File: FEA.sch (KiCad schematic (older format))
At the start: 18 parts

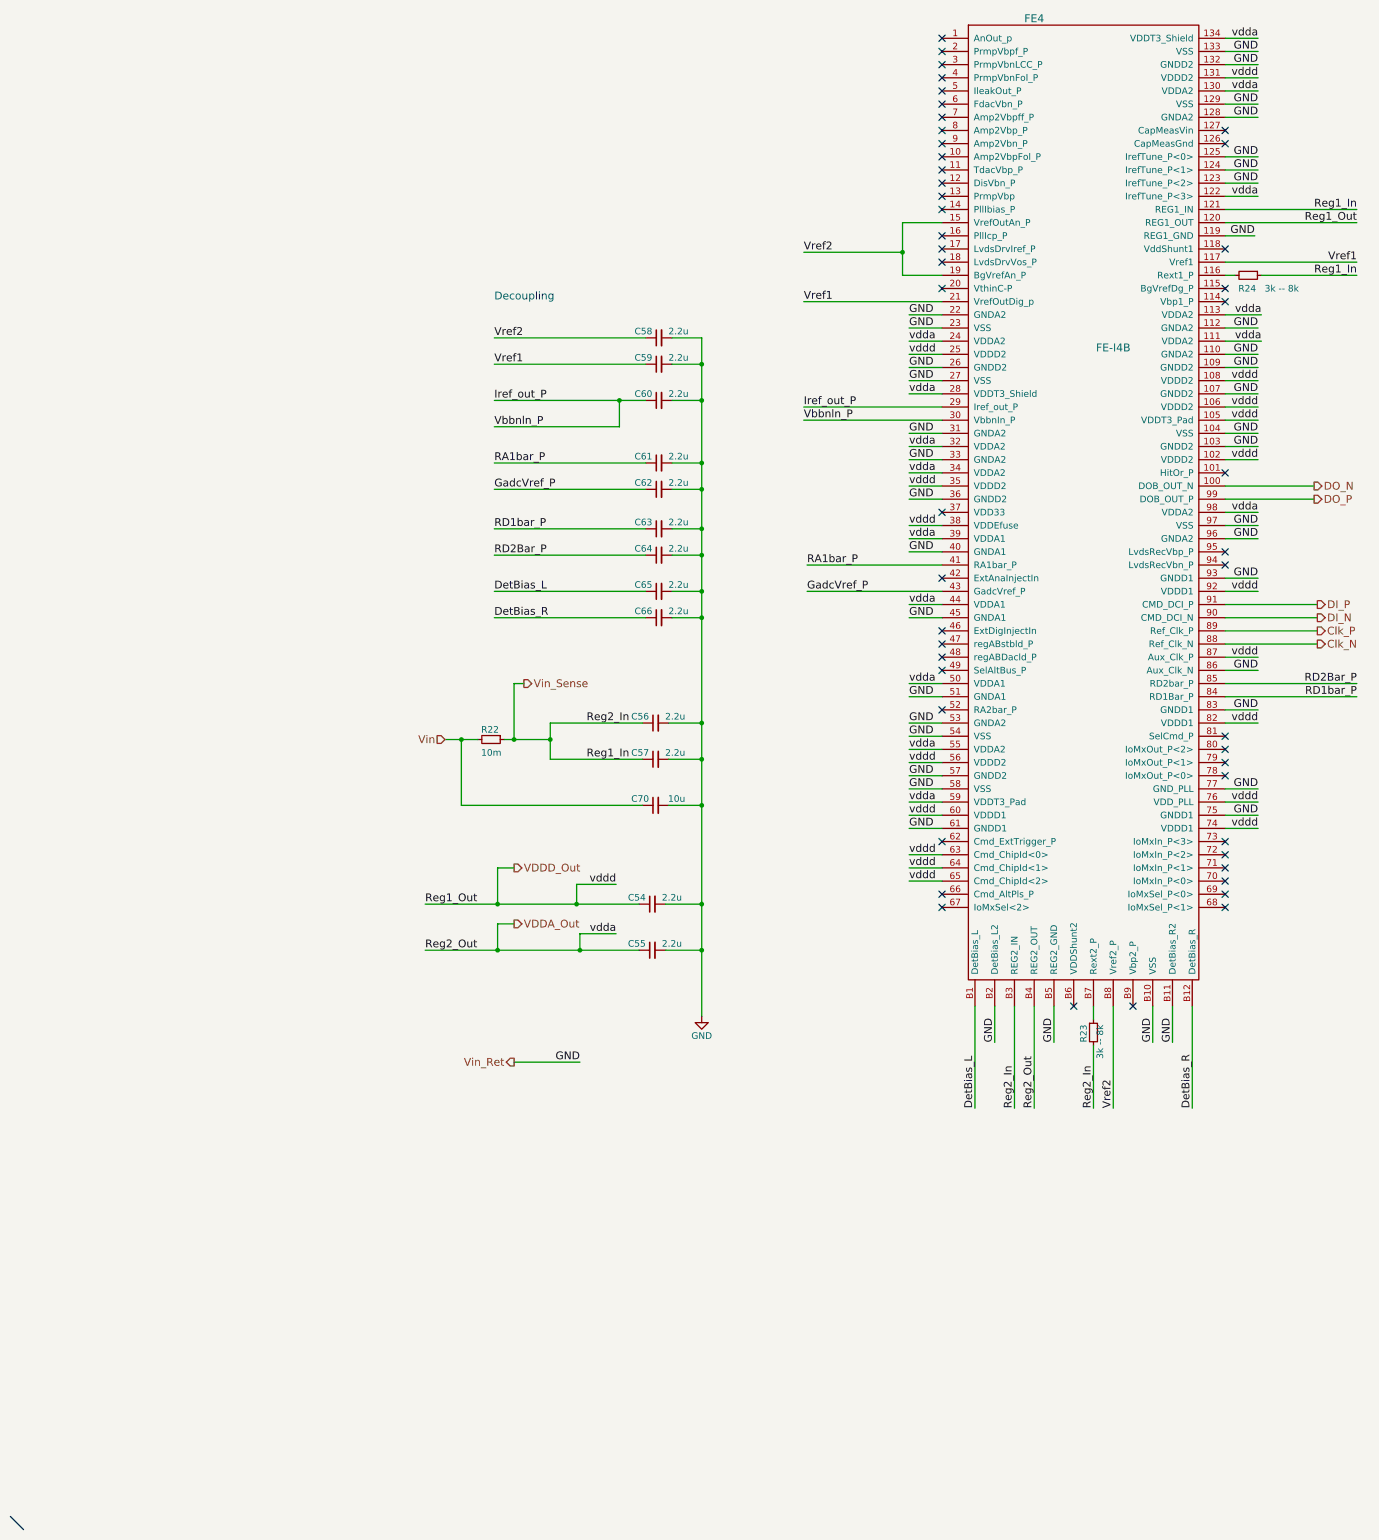
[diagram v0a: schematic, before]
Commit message: Edit decoupling cap values for V/I ref and Regulators
Signed-off-by: Katie Dunne <kdunne@mail.ccsf.edu>
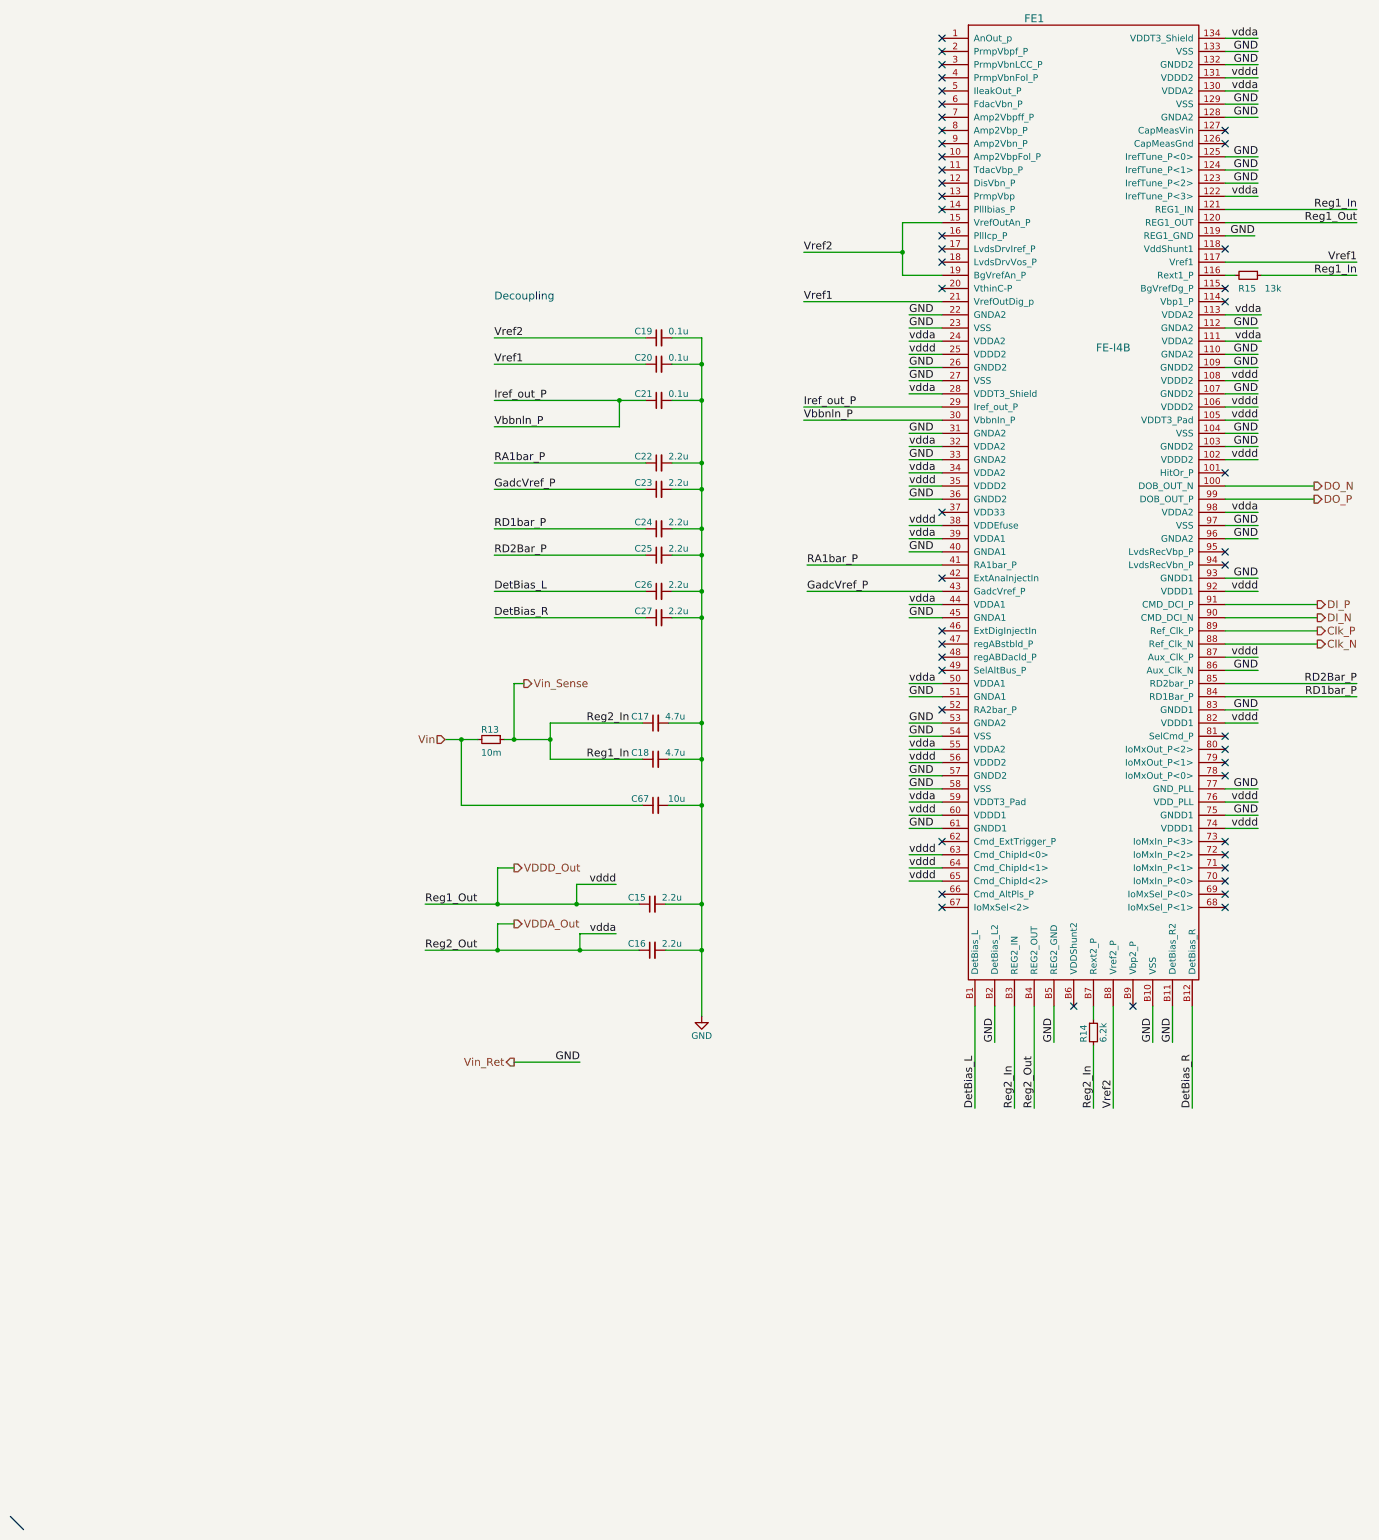
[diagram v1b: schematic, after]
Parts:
- C17, C18: value 2.2u -> 4.7u
- C19, C20, C21: value 2.2u -> 0.1u
- R14: value 3k -- 8k -> 6.2k
- R15: value 3k -- 8k -> 13k
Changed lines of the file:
@@
 $Descr A4 8268 11693 portrait
 encoding utf-8
-Sheet 5 5
+Sheet 2 5
 Title ""
 Date ""
@@
 AR Path="/58B026BA/589D45EA" Ref="FE3"  Part="1"
 AR Path="/58B026C4/589D45EA" Ref="FE4"  Part="1"
-F 0 "FE4" H 5225 4275 60  0000 C CNN
+F 0 "FE1" H 5225 4275 60  0000 C CNN
 F 1 "FE-I4B" H 5825 1775 60  0000 C CNN
 F 2 "module:WirebondPads" H 5825 2525 60  0001 C CNN
@@
 AR Path="/58B026BA/58AFC93B" Ref="R20"  Part="1"
 AR Path="/58B026C4/58AFC93B" Ref="R23"  Part="1"
-F 0 "R23" V 5600 8400 50  0000 L CNN
-F 1 "3k -- 8k" V 5725 8275 50  0000 L CNN
+F 0 "R14" V 5600 8400 50  0000 L CNN
+F 1 "6.2k" V 5750 8400 50  0000 L CNN
 F 2 "Resistors_SMD:R_0402" H 5675 8475 50  0001 C CNN
 F 3 "" H 5675 8475 50  0001 C CNN
@@
 AR Path="/58B026BA/58AFD85E" Ref="R21"  Part="1"
 AR Path="/58B026C4/58AFD85E" Ref="R24"  Part="1"
-F 0 "R24" V 6950 2650 50  0000 L CNN
-F 1 "3k -- 8k" V 6950 2850 50  0000 L CNN
+F 0 "R15" V 6950 2650 50  0000 L CNN
+F 1 "13k" V 6950 2850 50  0000 L CNN
 F 2 "Resistors_SMD:R_0402" H 6850 2725 50  0001 C CNN
 F 3 "" H 6850 2725 50  0001 C CNN
@@
 AR Path="/58B026BA/58BA4BDB" Ref="#PWR06"  Part="1"
 AR Path="/58B026C4/58BA4BDB" Ref="#PWR07"  Part="1"
-F 0 "#PWR07" H 2700 8100 50  0001 C CNN
+F 0 "#PWR04" H 2700 8100 50  0001 C CNN
 F 1 "GND" H 2700 8200 50  0000 C CNN
 F 2 "" H 2700 8350 50  0001 C CNN
@@
 AR Path="/58B026BA/58BA843C" Ref="C45"  Part="1"
 AR Path="/58B026C4/58BA843C" Ref="C58"  Part="1"
-F 0 "C58" V 2425 3250 50  0000 L CNN
-F 1 "2.2u" V 2425 2975 50  0000 L CNN
+F 0 "C19" V 2425 3250 50  0000 L CNN
+F 1 "0.1u" V 2425 2975 50  0000 L CNN
 F 2 "Capacitors_SMD:C_0402" H 2375 3200 50  0001 C CNN
 F 3 "" H 2375 3200 50  0001 C CNN
@@
 AR Path="/58B026BA/58B3509B" Ref="R19"  Part="1"
 AR Path="/58B026C4/58B3509B" Ref="R22"  Part="1"
-F 0 "R22" V 1025 6175 50  0000 L CNN
+F 0 "R13" V 1025 6175 50  0000 L CNN
 F 1 "10m" V 1200 6175 50  0000 L CNN
 F 2 "Resistors_SMD:R_0603" H 1100 6250 50  0001 C CNN
@@
 AR Path="/58B026BA/58B81EC6" Ref="C46"  Part="1"
 AR Path="/58B026C4/58B81EC6" Ref="C59"  Part="1"
-F 0 "C59" V 2425 3450 50  0000 L CNN
-F 1 "2.2u" V 2425 3175 50  0000 L CNN
+F 0 "C20" V 2425 3450 50  0000 L CNN
+F 1 "0.1u" V 2425 3175 50  0000 L CNN
 F 2 "Capacitors_SMD:C_0402" H 2375 3400 50  0001 C CNN
 F 3 "" H 2375 3400 50  0001 C CNN
@@
 AR Path="/58B026BA/58B81EFE" Ref="C47"  Part="1"
 AR Path="/58B026C4/58B81EFE" Ref="C60"  Part="1"
-F 0 "C60" V 2425 3725 50  0000 L CNN
-F 1 "2.2u" V 2425 3450 50  0000 L CNN
+F 0 "C21" V 2425 3725 50  0000 L CNN
+F 1 "0.1u" V 2425 3450 50  0000 L CNN
 F 2 "Capacitors_SMD:C_0402" H 2375 3675 50  0001 C CNN
 F 3 "" H 2375 3675 50  0001 C CNN
@@
 AR Path="/58B026BA/58B81F3D" Ref="C48"  Part="1"
 AR Path="/58B026C4/58B81F3D" Ref="C61"  Part="1"
-F 0 "C61" V 2425 4200 50  0000 L CNN
+F 0 "C22" V 2425 4200 50  0000 L CNN
 F 1 "2.2u" V 2425 3925 50  0000 L CNN
 F 2 "Capacitors_SMD:C_0402" H 2375 4150 50  0001 C CNN
@@
 AR Path="/58B026BA/58B81F93" Ref="C49"  Part="1"
 AR Path="/58B026C4/58B81F93" Ref="C62"  Part="1"
-F 0 "C62" V 2425 4400 50  0000 L CNN
+F 0 "C23" V 2425 4400 50  0000 L CNN
 F 1 "2.2u" V 2425 4125 50  0000 L CNN
 F 2 "Capacitors_SMD:C_0402" H 2375 4350 50  0001 C CNN
@@
 AR Path="/58B026BA/58B82007" Ref="C50"  Part="1"
 AR Path="/58B026C4/58B82007" Ref="C63"  Part="1"
-F 0 "C63" V 2425 4700 50  0000 L CNN
+F 0 "C24" V 2425 4700 50  0000 L CNN
 F 1 "2.2u" V 2425 4425 50  0000 L CNN
 F 2 "Capacitors_SMD:C_0402" H 2375 4650 50  0001 C CNN
@@
 AR Path="/58B026BA/58B82049" Ref="C51"  Part="1"
 AR Path="/58B026C4/58B82049" Ref="C64"  Part="1"
-F 0 "C64" V 2425 4900 50  0000 L CNN
+F 0 "C25" V 2425 4900 50  0000 L CNN
 F 1 "2.2u" V 2425 4625 50  0000 L CNN
 F 2 "Capacitors_SMD:C_0402" H 2375 4850 50  0001 C CNN
@@
 AR Path="/58B026BA/58B82086" Ref="C52"  Part="1"
 AR Path="/58B026C4/58B82086" Ref="C65"  Part="1"
-F 0 "C65" V 2425 5175 50  0000 L CNN
+F 0 "C26" V 2425 5175 50  0000 L CNN
 F 1 "2.2u" V 2425 4900 50  0000 L CNN
 F 2 "Capacitors_SMD:C_0402" H 2375 5125 50  0001 C CNN
@@
 AR Path="/58B026BA/58B820CA" Ref="C53"  Part="1"
 AR Path="/58B026C4/58B820CA" Ref="C66"  Part="1"
-F 0 "C66" V 2425 5375 50  0000 L CNN
+F 0 "C27" V 2425 5375 50  0000 L CNN
 F 1 "2.2u" V 2425 5100 50  0000 L CNN
 F 2 "Capacitors_SMD:C_0402" H 2375 5325 50  0001 C CNN
@@
 AR Path="/58B026BA/58B82111" Ref="C43"  Part="1"
 AR Path="/58B026C4/58B82111" Ref="C56"  Part="1"
-F 0 "C56" V 2400 6175 50  0000 L CNN
-F 1 "2.2u" V 2400 5900 50  0000 L CNN
+F 0 "C17" V 2400 6175 50  0000 L CNN
+F 1 "4.7u" V 2400 5900 50  0000 L CNN
 F 2 "Capacitors_SMD:C_0402" H 2350 6125 50  0001 C CNN
 F 3 "" H 2350 6125 50  0001 C CNN
@@
 AR Path="/58B026BA/58B82175" Ref="C44"  Part="1"
 AR Path="/58B026C4/58B82175" Ref="C57"  Part="1"
-F 0 "C57" V 2400 6450 50  0000 L CNN
-F 1 "2.2u" V 2400 6175 50  0000 L CNN
+F 0 "C18" V 2400 6450 50  0000 L CNN
+F 1 "4.7u" V 2400 6175 50  0000 L CNN
 F 2 "Capacitors_SMD:C_0402" H 2350 6400 50  0001 C CNN
 F 3 "" H 2350 6400 50  0001 C CNN
@@
 AR Path="/58B026BA/58B8280B" Ref="C41"  Part="1"
 AR Path="/58B026C4/58B8280B" Ref="C54"  Part="1"
-F 0 "C54" V 2375 7550 50  0000 L CNN
+F 0 "C15" V 2375 7550 50  0000 L CNN
 F 1 "2.2u" V 2375 7275 50  0000 L CNN
 F 2 "Capacitors_SMD:C_0402" H 2325 7500 50  0001 C CNN
@@
 AR Path="/58B026BA/58B82875" Ref="C42"  Part="1"
 AR Path="/58B026C4/58B82875" Ref="C55"  Part="1"
-F 0 "C55" V 2375 7900 50  0000 L CNN
+F 0 "C16" V 2375 7900 50  0000 L CNN
 F 1 "2.2u" V 2375 7625 50  0000 L CNN
 F 2 "Capacitors_SMD:C_0402" H 2325 7850 50  0001 C CNN
@@
 AR Path="/58B026BA/58C23965" Ref="C69"  Part="1"
 AR Path="/58B026C4/58C23965" Ref="C70"  Part="1"
-F 0 "C70" V 2400 6800 50  0000 L CNN
+F 0 "C67" V 2400 6800 50  0000 L CNN
 F 1 "10u" V 2400 6525 50  0000 L CNN
 F 2 "Capacitors_SMD:C_0603" H 2350 6750 50  0001 C CNN
